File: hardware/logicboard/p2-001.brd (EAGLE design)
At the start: 72 x 72 mm, 32 parts, among them IC1 5V, IC2 74LS07N, IC3 4066N, IC4 LTC485N, K1 G5V1, T1 2SC1815, U1 DS18B20

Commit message: Optimized PCB layout.
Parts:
- moved C6 19.0 mm to (30.0, 4.00)
- moved T1 18.0 mm to (36.0, 4.00)
- moved S1 14.0 mm to (18.0, 4.00)
- moved D2 1.00 mm to (18.0, 10.0)
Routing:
- net VOUT: track 118.6 -> 83.2 mm
- net L2: track 67.1 -> 42.9 mm, vias 0 -> 2
- net L1: track 68.4 -> 48.7 mm, vias 0 -> 1
- net VPULLUP: track 74.8 -> 94.3 mm, vias 4 -> 2
- net SDA: track 68.2 -> 84.6 mm
- net A3: track 37.5 -> 52.3 mm, vias 0 -> 1
- net RX: track 80.8 -> 67.7 mm
- net D2: track 79.0 -> 66.4 mm, vias 0 -> 1
- net N$5: track 31.3 -> 19.2 mm
- net D4: track 63.9 -> 51.8 mm, vias 0 -> 1
- net A4: track 53.0 -> 40.9 mm, vias 2 -> 4
- net MTX-: track 60.4 -> 71.6 mm
- net RLYSNK: track 18.9 -> 29.5 mm
- net SCL: track 83.2 -> 72.8 mm, vias 2 -> 0
- net GND: track 320.4 -> 310.8 mm, vias 3 -> 2
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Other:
- board text added: "Vpullup"

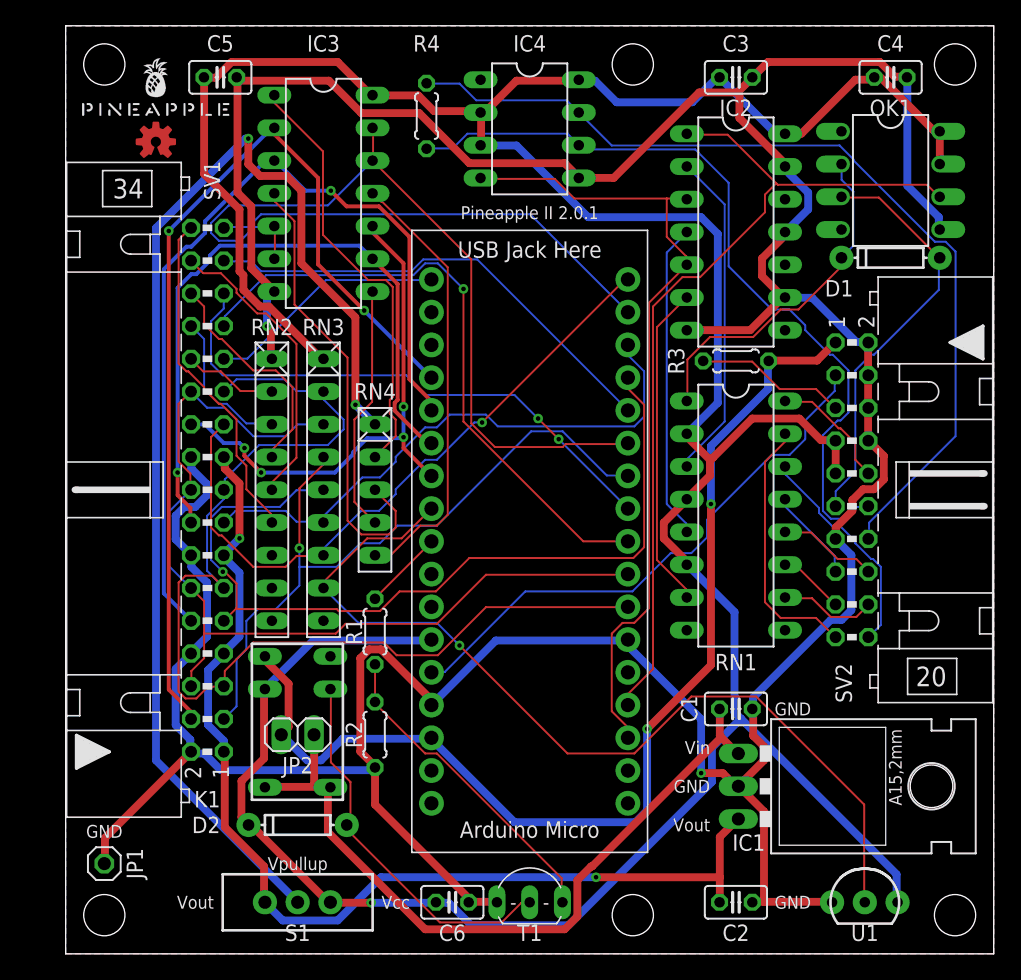
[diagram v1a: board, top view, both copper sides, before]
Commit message: Back LED is now connected to D13 (again).
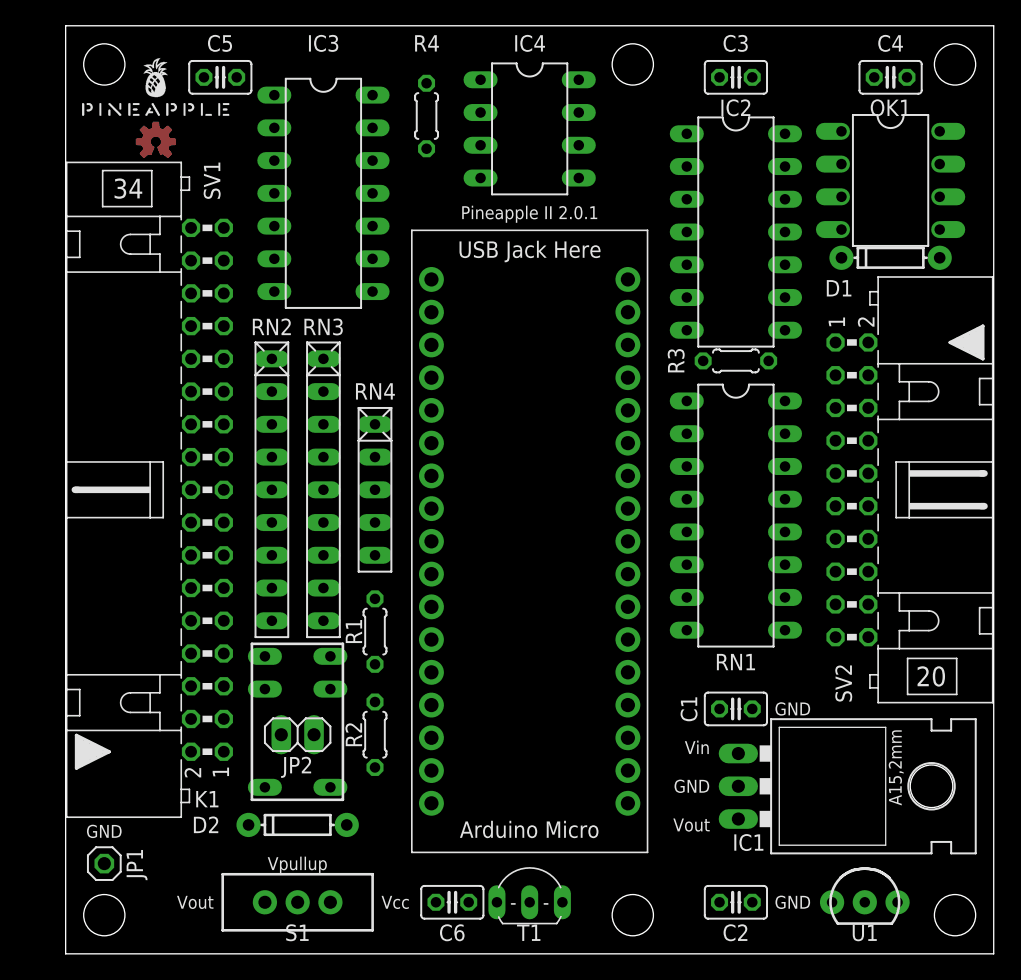
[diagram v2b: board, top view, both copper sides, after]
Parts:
- R3: value 1k -> 160
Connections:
- removed net L0: MC1.P$34, SV1.25
- removed net PWRLED: R3.1, SV2.5
- new net LED: MC1.P$34, R3.1
- new net LEDA: R3.2, SV2.5
- net VIN: no longer R3.2
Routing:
- net GND: track 310.8 -> 0.00 mm, vias 2 -> 0
- net VCC: track 272.2 -> 0.00 mm, vias 1 -> 0
- net VPULLUP: track 94.3 -> 0.00 mm, vias 2 -> 0
- net VIN: track 84.7 -> 0.00 mm, vias 2 -> 0
- net SDA: track 84.6 -> 0.00 mm
- net VOUT: track 83.2 -> 0.00 mm, vias 2 -> 0
- net A1: track 74.5 -> 0.00 mm, vias 2 -> 0
- net SCL: track 72.8 -> 0.00 mm
- net MTX-: track 71.6 -> 0.00 mm
- net THS: track 71.4 -> 0.00 mm, vias 1 -> 0
- net A2: track 67.8 -> 0.00 mm, vias 1 -> 0
- net RX: track 67.7 -> 0.00 mm
- net D2: track 66.4 -> 0.00 mm, vias 1 -> 0
- net PULLUP: track 62.7 -> 0.00 mm
- net TX: track 62.7 -> 0.00 mm
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- removed copper zone on layer 1, net GND
- removed copper zone on layer 16, net GND

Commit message: More change.
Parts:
- removed RN4: 10k, resistor-net:RN-5
- added J1: (no value), SparkFun-Connectors:JST-5-PTH
- added R5: 160, resistor:0204/5
- JP1: value GNDPIN -> PWR; device pinhead:1X01 -> pinhead:1X03
- R3: value 160 -> 120
- R4: value 120 -> 160
- RN2: value 330 -> 4.7k
- RN3: value 4.7k -> 10k; device resistor-net:RN-9 -> resistor-net:RN-5
- SV1: device con-ml:ML34L -> con-ml:ML26L
- moved U$1 57.0 mm to (8.00, 8.00), turned to 90 degrees
- moved LOGO1 39.6 mm to (36.0, 36.0)
- moved JP1 31.8 mm to (16.0, 36.0), turned to 90 degrees
- moved R4 31.2 mm to (52.0, 45.0), turned to 0 degrees
- moved R3 28.0 mm to (24.0, 47.0), turned to 90 degrees
- moved C4 19.8 mm to (49.0, 55.0), turned to 90 degrees
- moved C3 19.4 mm to (36.0, 57.0)
- moved OK1 19.4 mm to (45.0, 64.0)
- moved D1 13.4 mm to (52.0, 48.0)
- moved IC2 6.40 mm to (57.0, 60.0)
- moved RN2 4.00 mm to (20.0, 36.0)
- moved RN3 4.00 mm to (24.0, 36.0)
- moved IC4 3.00 mm to (33.0, 64.0)
- moved IC3 1.41 mm to (21.0, 60.0)
- moved C5 1.00 mm to (13.0, 68.0)
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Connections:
- net VIN renamed +12V
- removed net L0K: RN2.2, SV1.26
- removed net L1: MC1.P$9, SV1.27
- removed net L1K: RN2.3, SV1.28
- removed net L2: MC1.P$8, SV1.29
- removed net L2K: RN2.4, SV1.30
- removed net L3: MC1.P$5, SV1.31
- removed net L3K: RN2.5, SV1.32
- removed net L4: MC1.P$2, SV1.33
- removed net L4K: RN2.6, SV1.34
- new net FLED: MC1.P$2, SV1.25
- new net GPIO1: J1.3, MC1.P$9
- new net GPIO2: J1.4, MC1.P$8
- new net GPIO3: J1.5, MC1.P$5
- new net MOSI: J1.1, MC1.P$17
- new net N$1: R5.2, SV1.26
- new net SCLK: J1.2, MC1.P$18
- new net VDD: JP1.3, MC1.P$33
- net D1: now also RN2.4; no longer RN3.4
- net D2: now also RN2.5; no longer RN3.5
- net D3: now also RN2.6; no longer RN3.6
- net D4: now also RN2.7; no longer RN3.7
- net GND: now also JP1.2, R5.1; no longer JP1.1, RN2.1
- net LED: now also R4.1; no longer R3.1
- net LEDA: now also R4.2; no longer R3.2
- net MTX+: now also R3.1; no longer R4.1
- net MTX-: now also R3.2; no longer R4.2
- net N$3: now also RN3.2; no longer RN4.2
- net N$4: now also RN3.3; no longer RN4.3
- net N$5: now also RN3.4; no longer RN4.4
- net N$6: now also RN3.5; no longer RN4.5
- net SCL: now also RN2.3; no longer RN3.3
- net SDA: now also RN2.2; no longer RN3.2
- net THS: now also RN2.8; no longer RN3.8
- net VCC: now also JP1.1, RN2.1; no longer RN3.1
- net VPULLUP: now also RN3.1; no longer RN4.1
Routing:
- net VCC: track 0.00 -> 272.2 mm, vias 0 -> 4
- net GND: track 0.00 -> 266.4 mm
- net VOUT: track 0.00 -> 106.3 mm, vias 0 -> 4
- net SCLK: track 0.00 -> 98.3 mm
- net THS: track 0.00 -> 88.8 mm
- net TX: track 0.00 -> 87.9 mm
- net MTX-: track 0.00 -> 85.2 mm, vias 0 -> 3
- net A1: track 0.00 -> 84.7 mm
- net MTX+: track 0.00 -> 84.1 mm, vias 0 -> 1
- net +12V: track 0.00 -> 83.0 mm, vias 0 -> 1
- net SCL: track 0.00 -> 79.7 mm
- net SDA: track 0.00 -> 70.3 mm
- net MOSI: track 0.00 -> 67.3 mm
- net A2: track 0.00 -> 66.5 mm, vias 0 -> 1
- net D4: track 0.00 -> 64.3 mm
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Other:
- board text added: "2.0.1-X2"
- board text added: "Pineapple II"
- board text removed: "Pineapple II 2.0.1"

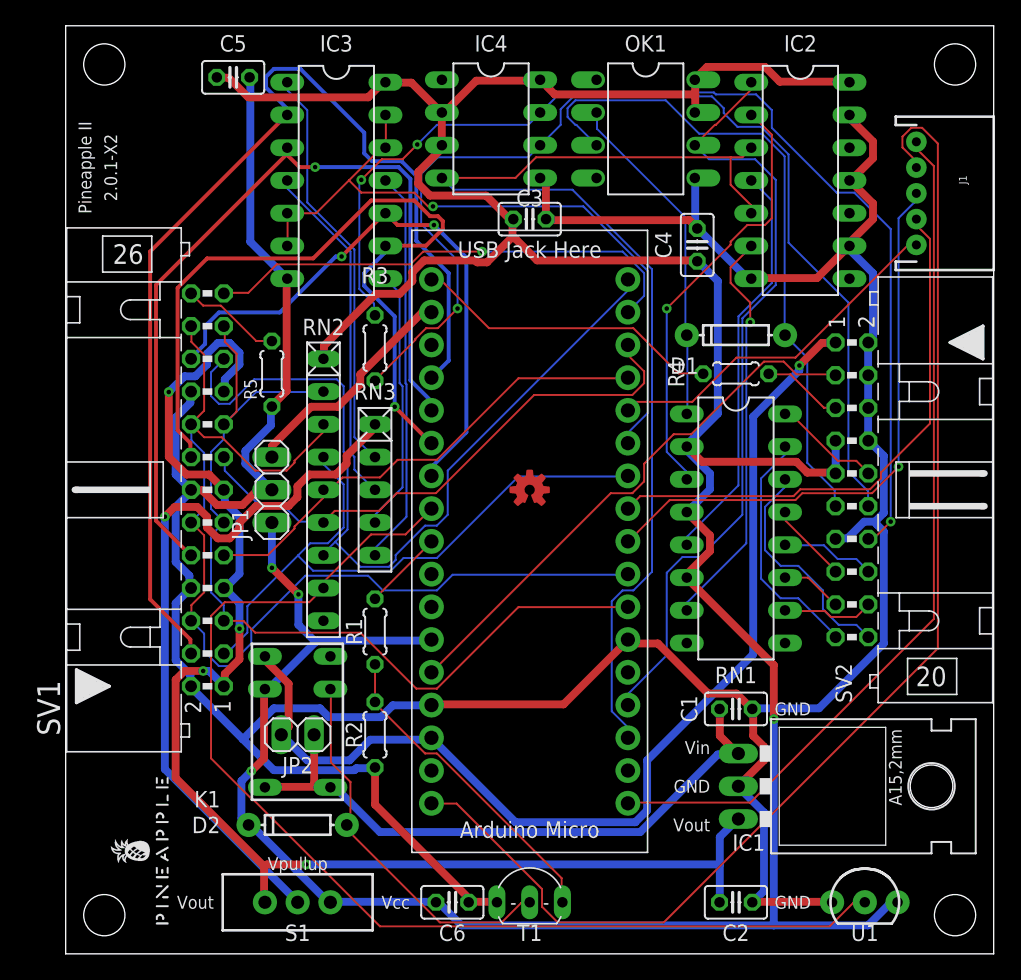
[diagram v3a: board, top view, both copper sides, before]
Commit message: Renumbered parts.
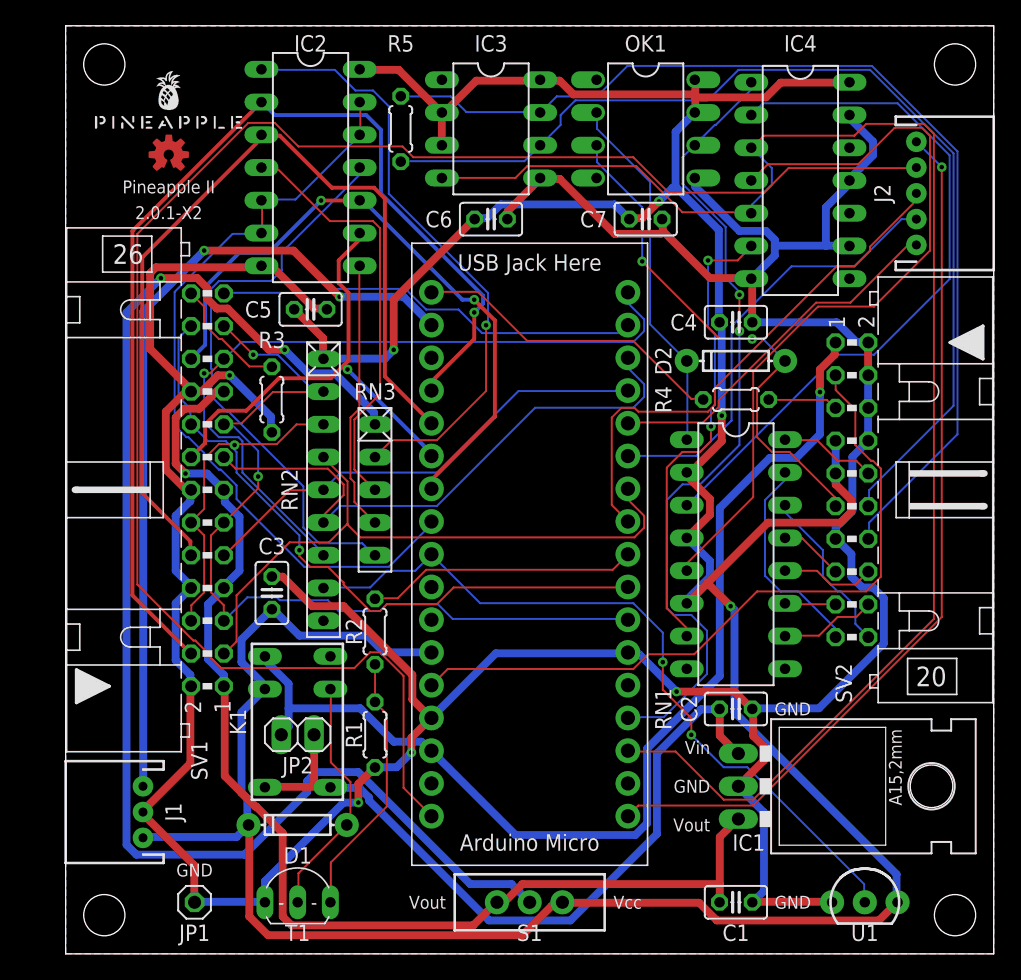
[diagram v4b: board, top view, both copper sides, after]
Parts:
- added C7: 103, rcl:C025-025X050
- added J2: (no value), SparkFun-Connectors:JST-5-PTH
- C1: value 104 -> 103
- C2: value 103 -> 104
- IC2: value 74LS07N -> 4066N; device 74xx-us:DIL14 -> 40xx:DIL14
- IC3: value 4066N -> LTC485N; device 40xx:DIL14 -> linear-technology:DIL08
- IC4: value LTC485N -> 74LS07N; device linear-technology:DIL08 -> 74xx-us:DIL14
- J1: device SparkFun-Connectors:JST-5-PTH -> SparkFun-Connectors:JST-3-PTH
- JP1: value PWR -> (none); device pinhead:1X03 -> pinhead:1X01
- R1: value 1k -> 47k
- R2: value 47k -> 1k
- R3: value 120 -> 160
- R5: value 160 -> 120
- moved J1 76.8 mm to (6.00, 11.0), turned to 90 degrees
- moved U$1 56.0 mm to (8.00, 64.0), turned to 0 degrees
- moved C6 53.1 mm to (33.0, 57.0)
- moved D1 51.0 mm to (18.0, 10.0)
- moved D2 49.5 mm to (52.0, 46.0)
- moved LOGO1 38.2 mm to (8.00, 62.0)
- moved IC2 38.0 mm to (19.0, 61.0)
- moved C3 35.2 mm to (16.0, 28.0), turned to 90 degrees
- moved JP1 32.6 mm to (10.0, 4.00), turned to 0 degrees
- moved IC4 24.3 mm to (57.0, 60.0)
- moved R5 21.5 mm to (26.0, 64.0)
- moved C5 19.0 mm to (19.0, 50.0)
- moved S1 18.0 mm to (36.0, 4.00)
- moved T1 18.0 mm to (18.0, 4.00)
- moved C1 15.0 mm to (52.0, 4.00)
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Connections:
- removed net N$1: R5.2, SV1.26
- new net FLEDK: R3.2, SV1.26
- net A1: now also IC2.2; no longer IC3.2
- net A2: now also IC2.3; no longer IC3.3
- net A3: now also IC2.9; no longer IC3.9
- net A4: now also IC2.10; no longer IC3.10
- net GND: now also C7.2, IC3.5, IC4.11, IC4.13, IC4.7, IC4.9, J1.2, JP1.1, R1.1, R3.1; no longer IC2.11, IC2.13, IC2.9, IC3.7, IC4.5, JP1.2, R2.1, R5.1
- net GPIO1: now also J2.3, MC1.P$8; no longer J1.3, MC1.P$9
- net GPIO2: now also J2.4, MC1.P$6; no longer J1.4, MC1.P$8
- net GPIO3: now also J2.5; no longer J1.5
- net MIDIINSND: now also D2.C; no longer D1.C
- net MIDIOUT2RTN: now also IC4.6; no longer IC2.6
- net MIDIOUTRTN: now also IC4.4; no longer IC2.4
- net MIDITHRURTN: now also IC4.2; no longer IC2.2
- net MINRTN: now also D2.A; no longer D1.A
- net MOSI: now also J2.1; no longer J1.1
- net MTX+: now also IC3.6, R5.1; no longer IC4.6, R3.1
- net MTX-: now also IC3.7, R5.2; no longer IC4.7, R3.2
- net N$3: now also IC2.1; no longer IC3.1
- net N$4: now also IC2.4; no longer IC3.4
- net N$5: now also IC2.8; no longer IC3.8
- net N$6: now also IC2.11; no longer IC3.11
- net PULLUP: now also IC2.12, IC2.13, IC2.5, IC2.6, MC1.P$27; no longer IC3.12, IC3.13, IC3.5, IC3.6, MC1.P$6
- net RLY: now also MC1.P$9, R2.2; no longer MC1.P$26, R1.2
- net RLYDRV: now also R1.2, R2.1; no longer R1.1, R2.2
- net RLYSNK: now also D1.A; no longer D2.A
- net RX: now also IC4.1; no longer IC2.1
- net SCLK: now also J2.2; no longer J1.2
- net THS: now also MC1.P$26; no longer MC1.P$27
- net TX: now also IC3.4, IC4.3, IC4.5; no longer IC2.3, IC2.5, IC4.4
- net V+12V: now also C2.1; no longer C1.1
- net VCC: now also C7.1, D1.C, IC3.2, IC3.3, IC3.8, IC4.14, J1.1; no longer D2.C, IC3.14, IC4.2, IC4.3, IC4.8, JP1.1
- net VDD: now also J1.3; no longer JP1.3
- net VOUT: now also C1.1; no longer C2.1
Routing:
- net VPULLUP: track 57.3 -> 106.3 mm, vias 1 -> 2
- net VDD: track 18.0 -> 63.6 mm, vias 0 -> 2
- net SCLK: track 98.3 -> 130.7 mm
- net THS: track 88.8 -> 58.4 mm, vias 0 -> 2
- net TX: track 87.9 -> 116.4 mm
- net MIDIOUTRTN: track 31.7 -> 59.9 mm
- net A3: track 61.4 -> 36.9 mm
- net MIDITHRURTN: track 33.8 -> 54.7 mm, vias 1 -> 0
- net GND: track 266.4 -> 286.8 mm, vias 0 -> 4
- net N$3: track 31.9 -> 47.2 mm, vias 0 -> 1
- net RLY: track 6.27 -> 21.1 mm
- net VCC: track 272.2 -> 286.6 mm
- net VOUT: track 106.3 -> 92.4 mm, vias 4 -> 1
- net N$6: track 30.8 -> 44.6 mm
- net RST: track 42.6 -> 55.5 mm
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- added copper zone on layer 1, net GND
- added copper zone on layer 16, net GND
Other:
- board text removed: "Vpullup"

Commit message: Silk.
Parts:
- moved R5 11.0 mm to (37.0, 64.0)
- moved C6 3.00 mm to (30.0, 57.0)
- moved IC3 3.00 mm to (30.0, 64.0)
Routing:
- net SCLK: track 130.7 -> 68.3 mm, vias 0 -> 2
- net VPULLUP: track 106.3 -> 69.0 mm, vias 2 -> 5
- net TX: track 116.4 -> 81.5 mm, vias 0 -> 3
- net V+12V: track 59.4 -> 88.4 mm
- net MINRTN: track 40.3 -> 67.7 mm, vias 2 -> 0
- net MTX-: track 80.9 -> 54.4 mm, vias 0 -> 2
- net RX: track 62.8 -> 86.4 mm, vias 2 -> 0
- net MIDIOUT2RTN: track 36.2 -> 49.5 mm, vias 2 -> 0
- net A2: track 68.6 -> 81.5 mm
- net A1: track 84.2 -> 96.9 mm
- net VCC: track 286.6 -> 274.2 mm, vias 4 -> 2
- net GPIO2: track 34.3 -> 46.2 mm, vias 0 -> 1
- net N$3: track 47.2 -> 36.5 mm, vias 1 -> 0
- net D1: track 49.1 -> 58.4 mm
- net N$6: track 44.6 -> 53.6 mm
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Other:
- board text added: "*Supply DC +12V."
- board text added: "3.3V"
- board text added: "5V"
- board text added: "IO1"
- board text added: "IO2"
- board text added: "IO3"
- board text added: "MOSI"
- board text added: "SCLK"

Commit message: Readability.
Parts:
- added JP3: RELAYJUMP, pinhead:1X02
- J1: value (none) -> Power
- J2: value (none) -> Display
- JP1: value (none) -> GNDPIN
- JP2: value (none) -> PWRSPL; device pinhead:1X02 -> pinhead:1X03
- S1: value (none) -> AnalogPullUpSelect
- moved JP2 30.3 mm to (48.0, 13.0), turned to 270 degrees
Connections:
- removed net FLEDK: R3.2, SV1.26
- removed net V+12V: C2.1, IC1.IN, JP2.2, K1.5, K1.6
- removed net VOUT: C1.1, IC1.OUT, S1.1, SV1.1, SV1.13, SV1.19, SV1.7
- new net +5V: C1.1, IC1.OUT, JP2.3, S1.1, SV1.1, SV1.13, SV1.19, SV1.7
- new net N$2: R3.1, SV1.26
- new net VIN: C2.1, IC1.IN, JP2.1, JP3.2, K1.5, K1.6
- net +12V: now also JP3.1; no longer JP2.1
- net GND: now also JP2.2, R3.2; no longer R3.1
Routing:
- net VOUT: track 100.8 -> 0.00 mm, vias 1 -> 0
- net +5V: track 0.00 -> 100.5 mm, vias 0 -> 1
- net V+12V: track 88.4 -> 0.00 mm
- net VIN: track 0.00 -> 58.0 mm
- net SCLK: track 68.3 -> 117.8 mm, vias 2 -> 0
- net MTX+: track 79.3 -> 51.2 mm
- net MINRTN: track 67.7 -> 40.3 mm, vias 0 -> 2
- net A3: track 37.7 -> 63.5 mm, vias 2 -> 1
- net RX: track 86.4 -> 61.1 mm, vias 0 -> 1
- net GPIO2: track 46.2 -> 31.1 mm
- net VPULLUP: track 69.0 -> 54.2 mm, vias 5 -> 1
- net A2: track 81.5 -> 66.8 mm, vias 0 -> 2
- net MTX-: track 54.4 -> 68.8 mm, vias 2 -> 0
- net RST: track 59.4 -> 45.3 mm
- net N$2: track 0.00 -> 13.6 mm
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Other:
- board text added: "*Bridge JP3 to bypass the relay K1."
- board text added: "Arduino's Vcc"
- board text added: "JP3"
- board text added: "Pull-up"
- board text added: "Regulated +5V"
- board text removed: "*Install JP2 to bypass the relay K1."
- board text removed: "JP2"
- board text removed: "Vin"
